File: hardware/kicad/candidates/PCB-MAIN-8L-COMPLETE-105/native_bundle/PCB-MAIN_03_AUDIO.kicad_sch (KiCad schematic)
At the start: 24 parts, among them U17 SN74LVC32APWR, U18 SN74AXC1T45DRLR, U19 4 channel 0.5 pF ESD, U20 4 channel 0.5 pF ESD, U21 4 channel 0.5 pF ESD, U22 4 channel 0.5 pF ESD, U7 SN74AXC8T245PWR

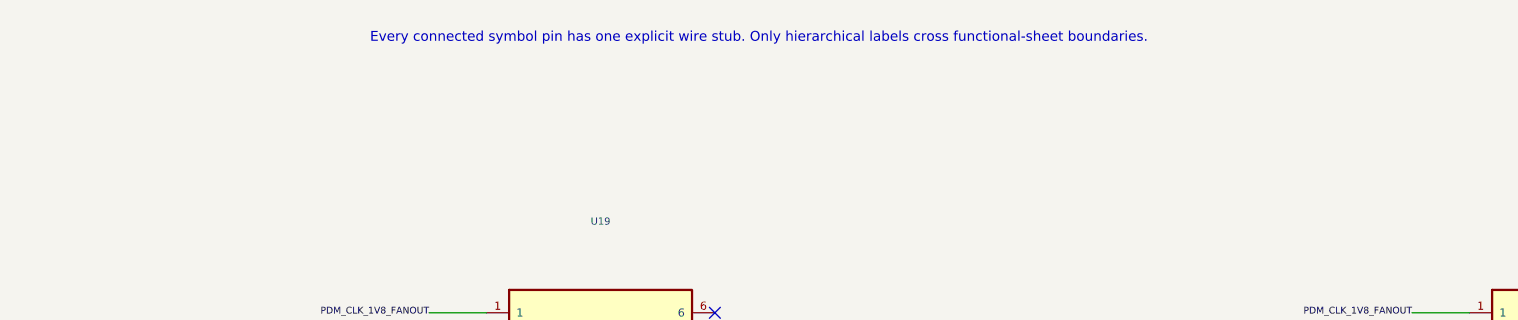
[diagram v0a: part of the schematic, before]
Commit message: PCB-MAIN Rev B: bilingual schematic notes and PDF
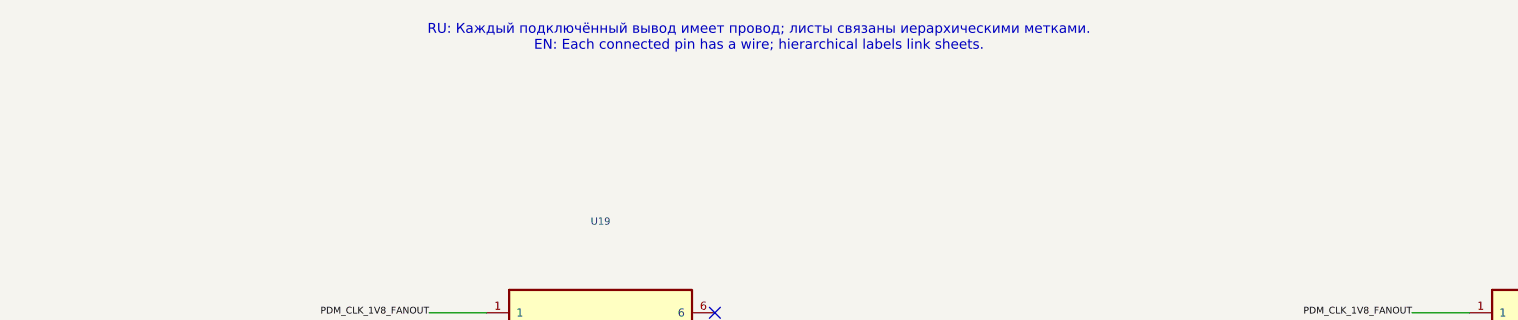
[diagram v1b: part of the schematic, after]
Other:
- note added: "RU: Каждый подключённый вывод имеет провод; листы связаны иерархическими метками. EN: Each connected pin has a wire; hierarchical labels link sheets."
- note removed: "Every connected symbol pin has one explicit wire stub. Only hierarchical labels cross functional-sheet boundaries."
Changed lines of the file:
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@@
     (stroke (width 0.0))
   )
-  (text "Every connected symbol pin has one explicit wire stub. Only hierarchical labels cross functional-sheet boundaries."
+  (text "RU: Каждый подключённый вывод имеет провод; листы связаны иерархическими метками.\nEN: Each connected pin has a wire; hierarchical labels link sheets."
     (at 297.0 12.7 0)
     (effects (font (size 1.1 1.1)))
